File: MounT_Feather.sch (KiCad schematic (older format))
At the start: 10 parts, among them J1 Teensy, J2 DB25_Male, U1 MAX3232

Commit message: remove unneeded dsr pulldowns, stagger pin rows
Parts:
- added S1: DS04-254-1L-01BK, 0_LOCAL:SW_DS04-254-1L-01BK, symbol 0_LOCAL:SW_DS04-254-1L-01BK
- J1: value Teensy -> Adafruit_Feather; footprint 0_LOCAL:Teensy35_36 -> 0_LOCAL:Adafruit_Feather; symbol 0_LOCAL:Teensy3.5 -> 0_LOCAL:Adafruit_Feather
- JP1: footprint 0_LOCAL:JP_H -> 0_LOCAL:PinHeader_1x02_P2.54mm_Horizontal
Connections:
- net labels added: En
- wire segments 43 -> 44
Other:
- note added: "S1: Optional. Only needed when attatching a lipo battery.\n[En]able has internal pullup.\nBoard is OFF when closed, ON when open.\nDIP Switch "ON" label will be misleading, so scratch it off.\nPCB silkscreen has ON/OFF labels."
- note removed: "Teensy 3.5, 3.6, 4.1"
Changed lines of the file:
@@
 encoding utf-8
 Sheet 1 1
-Title "MonT_Teensy - MCU on Model T, Teensy 3.5, 3.6, 4.1"
-Date "2020-08-26"
+Title "MonT_Feather - MCU on Model T, Adafruit Feather"
+Date "2020-08-19"
 Rev ""
 Comp "Brian K. White"
@@
 Text Notes 8470 2420 2    50   ~ 0
 TRS-80 Model 100
+$Comp
+L 0_LOCAL:Adafruit_Feather J1
+U 1 1 5F3C661A
+P 2550 4260
+F 0 "J1" H 2490 4380 60  0000 L CNN
+F 1 "Adafruit_Feather" V 2760 3930 60  0000 L CNN
+F 2 "0_LOCAL:Adafruit_Feather" H 925 2285 60  0001 L CNN
+F 3 "http://ww1.microchip.com/downloads/en/DeviceDoc/Atmel-7766-8-bit-AVR-ATmega16U4-32U4_Summary.pdf" H 925 2385 60  0001 L CNN
+F 4 "Active" H 2750 5460 60  0001 L CNN "Status"
+	1    2550 4260
+	-1   0    0    -1
+$EndComp
 Text Label 8210 3770 2    50   ~ 0
 DCD
@@
 	6900 4100 6300 4100
 Wire Wire Line
-	4700 4500 4100 4500
-Wire Wire Line
-	4100 4500 4100 2200
-Wire Wire Line
-	4700 4100 4200 4100
-Wire Wire Line
-	4200 2300 3300 2300
+	4700 4500 4200 4500
+Wire Wire Line
+	4200 4500 4200 3860
+Wire Wire Line
+	4200 3860 3150 3860
+Wire Wire Line
+	4700 4100 3800 4100
+Wire Wire Line
+	3800 4100 3800 3960
+Wire Wire Line
+	3800 3960 3150 3960
 $Comp
 L 0_LOCAL:GND #PWR04
@@
 $EndComp
 $Comp
+L 0_LOCAL:GND #PWR02
+U 1 1 5F47279A
+P 2650 5560
+F 0 "#PWR02" H 2650 5310 50  0001 C CNN
+F 1 "GND" V 2660 5380 50  0000 C CNN
+F 2 "" H 2650 5560 50  0001 C CNN
+F 3 "" H 2650 5560 50  0001 C CNN
+	1    2650 5560
+	1    0    0    -1
+$EndComp
+$Comp
 L 0_LOCAL:GND #PWR01
 U 1 1 5F472B1C
-P 1000 3300
-F 0 "#PWR01" H 1000 3050 50  0001 C CNN
-F 1 "GND" V 1000 3120 50  0000 C CNN
-F 2 "" H 1000 3300 50  0001 C CNN
-F 3 "" H 1000 3300 50  0001 C CNN
-	1    1000 3300
-	0    1    1    0
+P 2550 5560
+F 0 "#PWR01" H 2550 5310 50  0001 C CNN
+F 1 "GND" V 2560 5380 50  0000 C CNN
+F 2 "" H 2550 5560 50  0001 C CNN
+F 3 "" H 2550 5560 50  0001 C CNN
+	1    2550 5560
+	1    0    0    -1
 $EndComp
 $Comp
@@
 Text Label 6300 4500 0    50   ~ 0
 TXD
-Text Label 3300 2200 0    50   ~ 0
+Text Label 3150 3860 0    50   ~ 0
 RXD_TTL
-Text Label 3300 2300 0    50   ~ 0
+Text Label 3150 3960 0    50   ~ 0
 TXD_TTL
 Text Label 4700 4500 2    50   ~ 0
@@
 	0    1    1    0
 $EndComp
+$Comp
+L 0_LOCAL:SW_DS04-254-1L-01BK S1
+U 1 1 5F447651
+P 3600 5360
+F 0 "S1" H 3600 5500 50  0000 C CNN
+F 1 "DS04-254-1L-01BK" H 3600 5570 50  0001 C CNN
+F 2 "0_LOCAL:SW_DS04-254-1L-01BK" H 3600 5360 50  0001 L BNN
+F 3 "V0.0" H 3600 5360 50  0001 L BNN
+F 4 "CUI Inc." H 3600 5360 50  0001 L BNN "Field4"
+F 5 "3.96 mm" H 3600 5360 50  0001 L BNN "Field5"
+F 6 "Manufacturer Recommendations" H 3600 5360 50  0001 L BNN "Field6"
+	1    3600 5360
+	1    0    0    -1
+$EndComp
+Wire Wire Line
+	3150 5360 3300 5360
+$Comp
+L 0_LOCAL:GND #PWR0103
+U 1 1 5F44ACEF
+P 3900 5360
+F 0 "#PWR0103" H 3900 5110 50  0001 C CNN
+F 1 "GND" H 3950 5170 50  0000 C CNN
+F 2 "" H 3900 5360 50  0001 C CNN
+F 3 "" H 3900 5360 50  0001 C CNN
+	1    3900 5360
+	1    0    0    -1
+$EndComp
+Text Label 3150 5360 0    50   ~ 0
+En
 Wire Wire Line
 	7000 3600 6800 3600
@@
 	1    0    0    -1
 $EndComp
+Text Notes 3180 6100 0    50   ~ 0
+S1: Optional. Only needed when attatching a lipo battery.\n[En]able has internal pullup.\nBoard is OFF when closed, ON when open.\nDIP Switch "ON" label will be misleading, so scratch it off.\nPCB silkscreen has ON/OFF labels.
 $Comp
 L 0_LOCAL:Jumper_2_Bridged JP1
 U 1 1 5F3DBD1F
 P 7970 4370
-F 0 "JP1" H 7850 4430 50  0000 C CNN
+F 0 "JP1" H 7970 4350 50  0000 C CNN
 F 1 "Jumper_2_Bridged" H 8000 4480 50  0001 C CNN
-F 2 "0_LOCAL:JP_H" H 7970 4370 50  0001 C CNN
+F 2 "0_LOCAL:PinHeader_1x02_P2.54mm_Horizontal" H 7970 4370 50  0001 C CNN
 F 3 "~" H 7970 4370 50  0001 C CNN
 	1    7970 4370
-	1    0    0    -1
+	-1   0    0    -1
 $EndComp
 Wire Wire Line
@@
 Wire Wire Line
 	7770 4570 7770 4370
+$Comp
+L 0_LOCAL:+3V3 #PWR0106
+U 1 1 5F3FB811
+P 2050 3460
+F 0 "#PWR0106" H 2050 3310 50  0001 C CNN
+F 1 "+3V3" H 2030 3600 50  0000 C CNN
+F 2 "" H 2050 3460 50  0001 C CNN
+F 3 "" H 2050 3460 50  0001 C CNN
+	1    2050 3460
+	1    0    0    -1
+$EndComp
 $Comp
 L 0_LOCAL:+3V3 #PWR0107
@@
 DSR
 Wire Wire Line
-	4000 4300 4700 4300
+	3150 4360 3800 4360
+Wire Wire Line
+	3800 4360 3800 4300
+Wire Wire Line
+	3800 4300 4700 4300
+Text Label 3150 4360 0    50   ~ 0
+DTR_TTL
 Text Label 4700 4300 2    50   ~ 0
 DTR_TTL
 Wire Wire Line
-	4700 4700 3900 4700
-Wire Wire Line
-	3900 4700 3900 2600
-Text Label 3300 2600 0    50   ~ 0
+	4700 4700 3800 4700
+Wire Wire Line
+	3800 4700 3800 4460
+Text Label 3150 4460 0    50   ~ 0
 DSR_TTL
 Text Label 4700 4700 2    50   ~ 0
@@
 	7770 4120 7770 4170
 Wire Wire Line
-	4200 4100 4200 2300
-Wire Wire Line
-	4000 2500 4000 4300
-Text Label 3300 2500 0    50   ~ 0
-DTR_TTL
-$Comp
-L 0_LOCAL:Teensy3.5 J1
-U 1 1 5F3C661A
-P 2150 4250
-F 0 "J1" H 2090 4370 60  0000 L CNN
-F 1 "Teensy" V 2360 3920 60  0000 L CNN
-F 2 "0_LOCAL:Teensy35_36" H 525 2275 60  0001 L CNN
-F 3 "" H 525 2375 60  0001 L CNN
-F 4 "Active" H 2350 5450 60  0001 L CNN "Status"
-	1    2150 4250
-	-1   0    0    -1
-$EndComp
-Wire Wire Line
-	3300 2200 4100 2200
-Wire Wire Line
-	4000 2500 3300 2500
-$Comp
-L 0_LOCAL:GND #PWR0103
-U 1 1 5F4DCEBD
-P 1000 4400
-F 0 "#PWR0103" H 1000 4150 50  0001 C CNN
-F 1 "GND" V 1000 4220 50  0000 C CNN
-F 2 "" H 1000 4400 50  0001 C CNN
-F 3 "" H 1000 4400 50  0001 C CNN
-	1    1000 4400
-	0    1    1    0
-$EndComp
-$Comp
-L 0_LOCAL:GND #PWR0109
-U 1 1 5F4DE306
-P 1000 4500
-F 0 "#PWR0109" H 1000 4250 50  0001 C CNN
-F 1 "GND" V 1000 4320 50  0000 C CNN
-F 2 "" H 1000 4500 50  0001 C CNN
-F 3 "" H 1000 4500 50  0001 C CNN
-	1    1000 4500
-	0    1    1    0
-$EndComp
-$Comp
-L 0_LOCAL:GND #PWR0110
-U 1 1 5F4DEB4B
-P 1000 4600
-F 0 "#PWR0110" H 1000 4350 50  0001 C CNN
-F 1 "GND" V 1000 4420 50  0000 C CNN
-F 2 "" H 1000 4600 50  0001 C CNN
-F 3 "" H 1000 4600 50  0001 C CNN
-	1    1000 4600
-	0    1    1    0
-$EndComp
-$Comp
-L 0_LOCAL:GND #PWR0111
-U 1 1 5F4ED9FD
-P 3300 4700
-F 0 "#PWR0111" H 3300 4450 50  0001 C CNN
-F 1 "GND" V 3300 4520 50  0000 C CNN
-F 2 "" H 3300 4700 50  0001 C CNN
-F 3 "" H 3300 4700 50  0001 C CNN
-	1    3300 4700
-	0    -1   -1   0
-$EndComp
-$Comp
-L 0_LOCAL:GND #PWR0112
-U 1 1 5F4F2490
-P 3300 5900
-F 0 "#PWR0112" H 3300 5650 50  0001 C CNN
-F 1 "GND" V 3300 5720 50  0000 C CNN
-F 2 "" H 3300 5900 50  0001 C CNN
-F 3 "" H 3300 5900 50  0001 C CNN
-	1    3300 5900
-	0    -1   -1   0
-$EndComp
-$Comp
-L 0_LOCAL:GND #PWR0115
-U 1 1 5F4FFFE7
-P 3300 2100
-F 0 "#PWR0115" H 3300 1850 50  0001 C CNN
-F 1 "GND" V 3300 1920 50  0000 C CNN
-F 2 "" H 3300 2100 50  0001 C CNN
-F 3 "" H 3300 2100 50  0001 C CNN
-	1    3300 2100
-	0    -1   -1   0
-$EndComp
-$Comp
-L 0_LOCAL:+3V3 #PWR0116
-U 1 1 5F505253
-P 1000 5800
-F 0 "#PWR0116" H 1000 5650 50  0001 C CNN
-F 1 "+3V3" V 990 6000 50  0000 C CNN
-F 2 "" H 1000 5800 50  0001 C CNN
-F 3 "" H 1000 5800 50  0001 C CNN
-	1    1000 5800
-	0    -1   -1   0
-$EndComp
-Text Notes 2400 1630 2    50   ~ 0
-Teensy 3.5, 3.6, 4.1
-Wire Wire Line
-	3300 2600 3900 2600
+	3150 4460 3800 4460
 $EndSCHEMATC

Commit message: remove unused models, update readme
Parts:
- J1: footprint 0_LOCAL:Adafruit_Feather -> 0_LOCAL:Adafruit_Feather_stagger
- S1: footprint 0_LOCAL:SW_DS04-254-1L-01BK -> 0_LOCAL:CSS-121xC; symbol 0_LOCAL:SW_DS04-254-1L-01BK -> 0_LOCAL:CSS-1210xC
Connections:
- net labels added: CTS_232, DCD_232, DSR_232, DTR_232, RI_232, RTS_232, RX_232, RX_TTL, TX_232, TX_TTL
- net labels removed: CTS, DCD, DSR, DTR, RI, RTS, RXD, RXD_TTL, TXD, TXD_TTL
- wire segments 44 -> 45
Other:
- note added: "S1 is optional. Only needed when attatching a lipo battery.\n[En]able has internal pullup.\nBoard is OFF when closed (to GND), ON when open."
- note removed: "S1: Optional. Only needed when attatching a lipo battery.\n[En]able has internal pullup.\nBoard is OFF when closed, ON when open.\nDIP Switch "ON" label will be misleading, so scratch it off.\nPCB silkscreen has ON/OFF labels."
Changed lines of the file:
@@
 encoding utf-8
 Sheet 1 1
-Title "MonT_Feather - MCU on Model T, Adafruit Feather"
+Title "Feather MounT - Adafruit Feather on Model T serial port"
 Date "2020-08-19"
 Rev ""
@@
 $EndDescr
 Text Label 8210 4970 2    50   ~ 0
-TXD
+TX_232
 Text Label 8210 4770 2    50   ~ 0
-RXD
+RX_232
 Text Label 8210 4570 2    50   ~ 0
-RTS
+RTS_232
 Text Label 8210 4370 2    50   ~ 0
-CTS
+CTS_232
 Text Label 8210 4170 2    50   ~ 0
-DSR
+DSR_232
 Text Label 8210 3870 2    50   ~ 0
-DTR
+DTR_232
 Text Label 8210 3470 2    50   ~ 0
-RI
+RI_232
 Text Notes 8470 2420 2    50   ~ 0
 TRS-80 Model 100
@@
 F 0 "J1" H 2490 4380 60  0000 L CNN
 F 1 "Adafruit_Feather" V 2760 3930 60  0000 L CNN
-F 2 "0_LOCAL:Adafruit_Feather" H 925 2285 60  0001 L CNN
+F 2 "0_LOCAL:Adafruit_Feather_stagger" H 925 2285 60  0001 L CNN
 F 3 "http://ww1.microchip.com/downloads/en/DeviceDoc/Atmel-7766-8-bit-AVR-ATmega16U4-32U4_Summary.pdf" H 925 2385 60  0001 L CNN
 F 4 "Active" H 2750 5460 60  0001 L CNN "Status"
@@
 $EndComp
 Text Label 8210 3770 2    50   ~ 0
-DCD
+DCD_232
 $Comp
 L 0_LOCAL:Connector_DB25_Male J2
@@
 $EndComp
 Text Label 6300 4100 0    50   ~ 0
-RXD
+RX_232
 Text Label 6300 4500 0    50   ~ 0
-TXD
+TX_232
 Text Label 3150 3860 0    50   ~ 0
-RXD_TTL
+RX_TTL
 Text Label 3150 3960 0    50   ~ 0
-TXD_TTL
+TX_TTL
 Text Label 4700 4500 2    50   ~ 0
-RXD_TTL
+RX_TTL
 Text Label 4700 4100 2    50   ~ 0
-TXD_TTL
+TX_TTL
 $Comp
 L 0_LOCAL:GND #PWR0102
@@
 	0    1    1    0
 $EndComp
-$Comp
-L 0_LOCAL:SW_DS04-254-1L-01BK S1
-U 1 1 5F447651
-P 3600 5360
-F 0 "S1" H 3600 5500 50  0000 C CNN
-F 1 "DS04-254-1L-01BK" H 3600 5570 50  0001 C CNN
-F 2 "0_LOCAL:SW_DS04-254-1L-01BK" H 3600 5360 50  0001 L BNN
-F 3 "V0.0" H 3600 5360 50  0001 L BNN
-F 4 "CUI Inc." H 3600 5360 50  0001 L BNN "Field4"
-F 5 "3.96 mm" H 3600 5360 50  0001 L BNN "Field5"
-F 6 "Manufacturer Recommendations" H 3600 5360 50  0001 L BNN "Field6"
-	1    3600 5360
-	1    0    0    -1
-$EndComp
-Wire Wire Line
-	3150 5360 3300 5360
-$Comp
-L 0_LOCAL:GND #PWR0103
-U 1 1 5F44ACEF
-P 3900 5360
-F 0 "#PWR0103" H 3900 5110 50  0001 C CNN
-F 1 "GND" H 3950 5170 50  0000 C CNN
-F 2 "" H 3900 5360 50  0001 C CNN
-F 3 "" H 3900 5360 50  0001 C CNN
-	1    3900 5360
-	1    0    0    -1
-$EndComp
 Text Label 3150 5360 0    50   ~ 0
 En
@@
 	1    0    0    -1
 $EndComp
-Text Notes 3180 6100 0    50   ~ 0
-S1: Optional. Only needed when attatching a lipo battery.\n[En]able has internal pullup.\nBoard is OFF when closed, ON when open.\nDIP Switch "ON" label will be misleading, so scratch it off.\nPCB silkscreen has ON/OFF labels.
+Text Notes 2940 5850 0    50   ~ 0
+S1 is optional. Only needed when attatching a lipo battery.\n[En]able has internal pullup.\nBoard is OFF when closed (to GND), ON when open.
 $Comp
 L 0_LOCAL:Jumper_2_Bridged JP1
@@
 	7600 4700 6300 4700
 Text Label 6300 4300 0    50   ~ 0
-DSR
+DSR_232
 Wire Wire Line
 	3150 4360 3800 4360
@@
 	7770 4170 8210 4170
 Text Label 6300 4700 0    50   ~ 0
-DTR
+DTR_232
 Wire Wire Line
 	7770 3770 8210 3770
@@
 Wire Wire Line
 	3150 4460 3800 4460
+Wire Wire Line
+	3150 5360 3400 5360
+Wire Wire Line
+	3800 5260 3850 5260
+$Comp
+L 0_LOCAL:GND #PWR0103
+U 1 1 5F44ACEF
+P 3850 5260
+F 0 "#PWR0103" H 3850 5010 50  0001 C CNN
+F 1 "GND" H 3900 5070 50  0000 C CNN
+F 2 "" H 3850 5260 50  0001 C CNN
+F 3 "" H 3850 5260 50  0001 C CNN
+	1    3850 5260
+	1    0    0    -1
+$EndComp
+$Comp
+L 0_LOCAL:CSS-1210xC S1
+U 1 1 5F447651
+P 3600 5260
+F 0 "S1" H 3600 5400 50  0000 C CNN
+F 1 "DS04-254-1L-01BK" H 3600 5470 50  0001 C CNN
+F 2 "0_LOCAL:CSS-121xC" H 3600 5260 50  0001 L BNN
+F 3 "V0.0" H 3600 5260 50  0001 L BNN
+F 4 "CUI Inc." H 3600 5260 50  0001 L BNN "Field4"
+F 5 "3.96 mm" H 3600 5260 50  0001 L BNN "Field5"
+F 6 "Manufacturer Recommendations" H 3600 5260 50  0001 L BNN "Field6"
+	1    3600 5260
+	-1   0    0    -1
+$EndComp
 $EndSCHEMATC

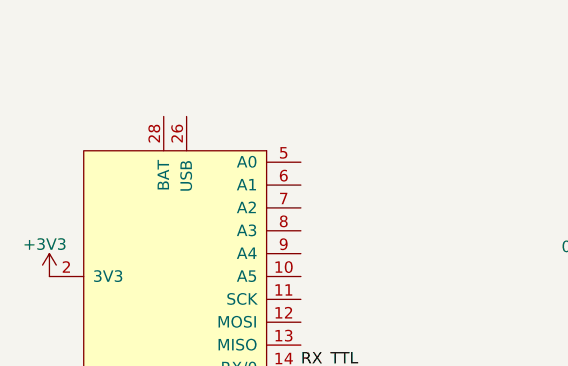
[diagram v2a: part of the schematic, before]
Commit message: Teensy BOM missing jumper
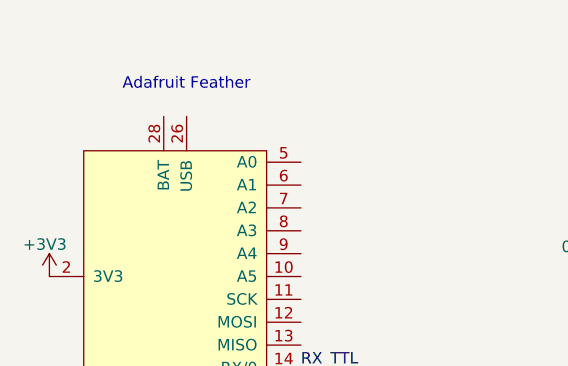
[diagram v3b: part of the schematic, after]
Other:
- note added: "Adafruit Feather"
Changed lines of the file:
@@
 	-1   0    0    -1
 $EndComp
+Text Notes 2930 2650 2    50   ~ 0
+Adafruit Feather
 $EndSCHEMATC
